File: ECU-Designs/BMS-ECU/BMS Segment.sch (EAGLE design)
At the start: 94 parts, among them Q10 P-CHANNEL_MOSFET, Q11 P-CHANNEL_MOSFET, Q12 P-CHANNEL_MOSFET, Q13 P-CHANNEL_MOSFET, Q2 P-CHANNEL_MOSFET, Q3 P-CHANNEL_MOSFET, Q4 P-CHANNEL_MOSFET, Q5 P-CHANNEL_MOSFET, Q6 P-CHANNEL_MOSFET, Q7 P-CHANNEL_MOSFET, Q8 P-CHANNEL_MOSFET, Q9 P-CHANNEL_MOSFET

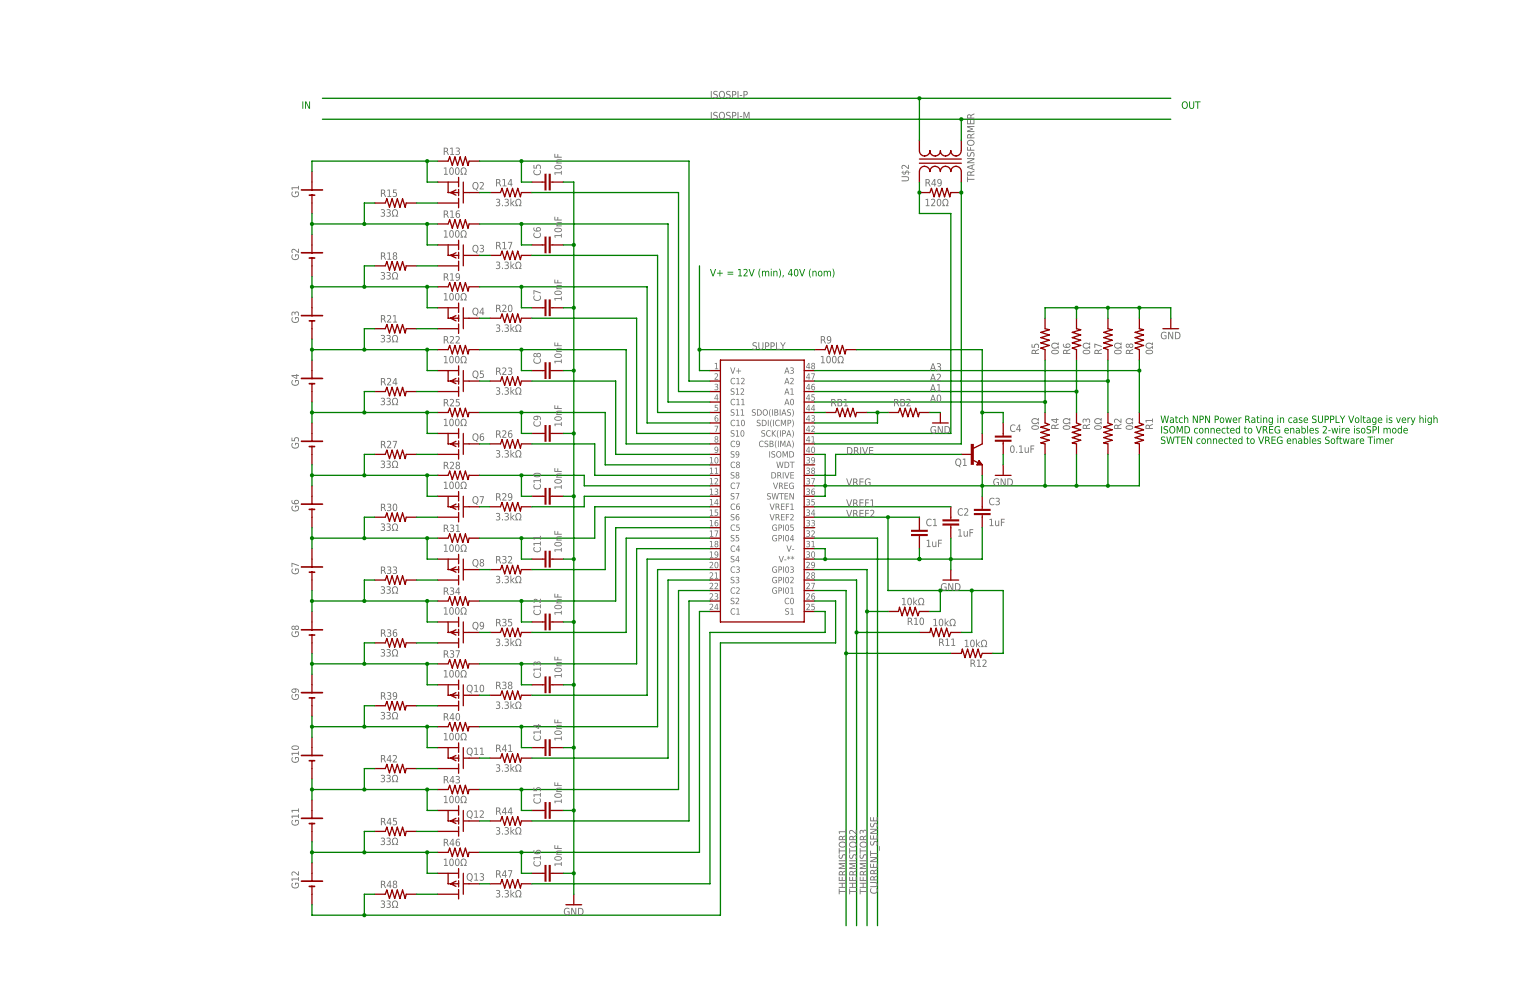
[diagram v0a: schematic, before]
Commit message: Updated BMS segment & created BMS Microcontroller
Updated BMS segment schematic to to reflect that the LTC6804 is powered
from the cells it is monitoring.  Also added connectors.  Created a
preliminary design for the microcontroller board that will process the
BMS data from all the BMS segment boards.  Some resistor values and pin
assignments still need to be determined.
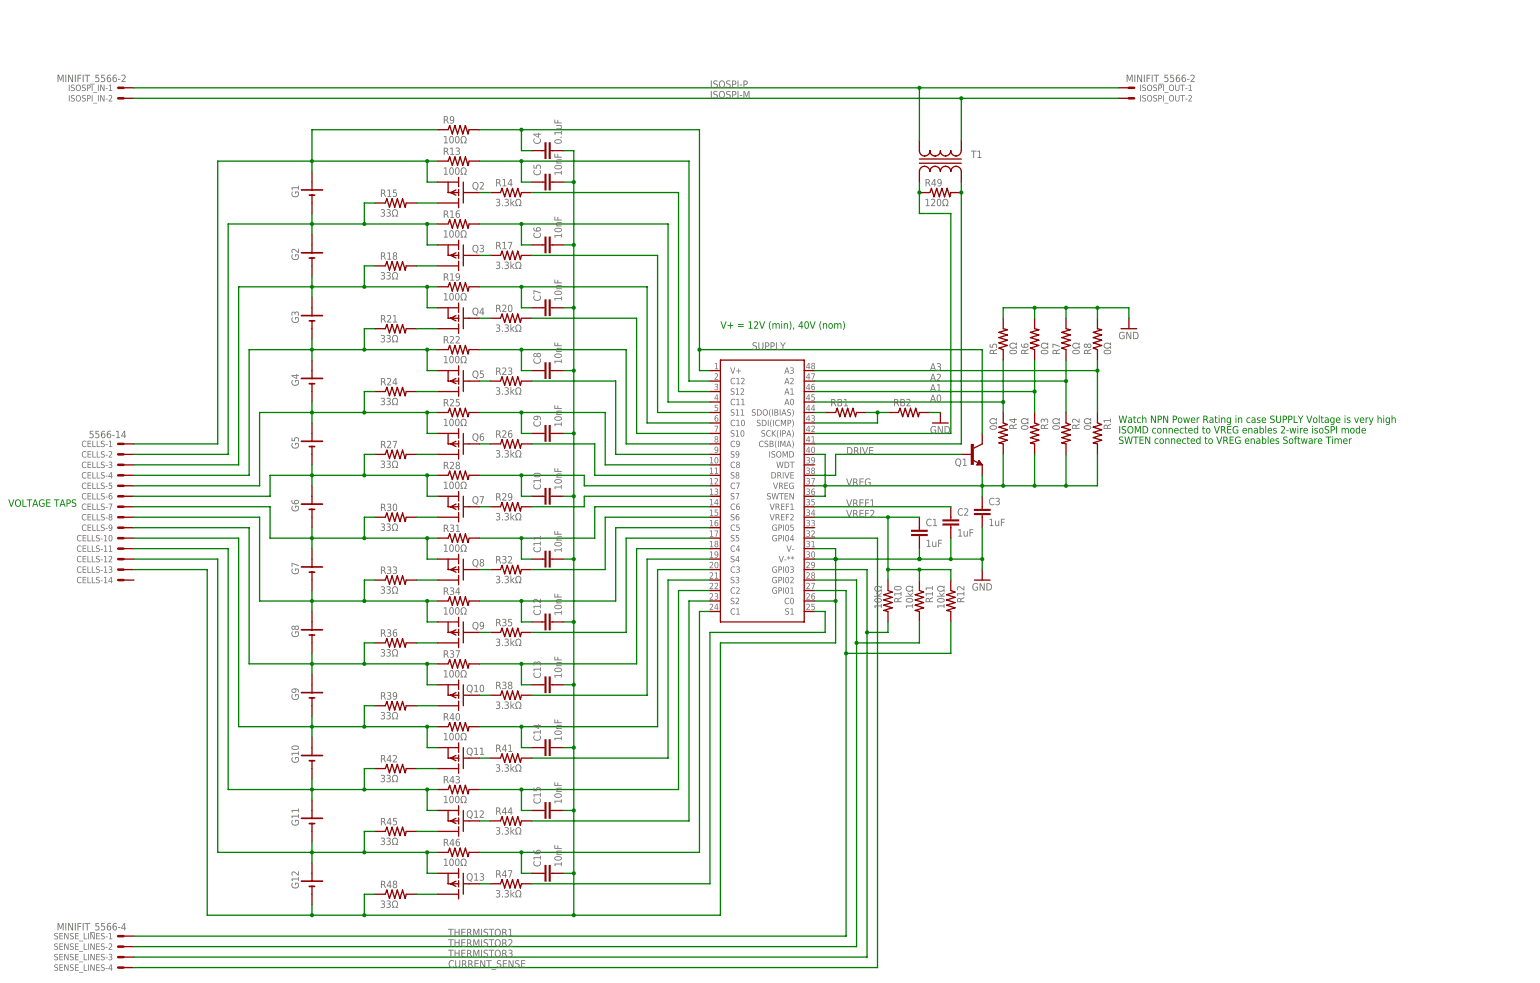
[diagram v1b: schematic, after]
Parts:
- added CELLS: 5566-14, con-molex:5566-14
- added ISOSPI_IN, ISOSPI_OUT: MINIFIT_5566-2, HyTechDevices:MINIFIT_5566-2
- added SENSE_LINES: MINIFIT_5566-4, HyTechDevices:MINIFIT_5566-4
- renumbered U$2 to T1
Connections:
- removed net N$5: C4.1, Q1.COLLECTOR, R9.2
- removed net N$67: G12.-, R48.1, U$1.C0
- net CURRENT_SENSE: now also SENSE_LINES-4.S
- net GND: now also CELLS-13.S, G12.-, R48.1, U$1.C0
- net ISOSPI-M: now also ISOSPI_IN-2.S, ISOSPI_OUT-2.S
- net ISOSPI-P: now also ISOSPI_IN-1.S, ISOSPI_OUT-1.S
- net N$19: now also CELLS-2.S
- net N$21: now also CELLS-3.S
- net N$26: now also CELLS-4.S
- net N$3: now also CELLS-1.S, R9.1
- net N$33: now also CELLS-5.S
- net N$37: now also CELLS-6.S
- net N$41: now also CELLS-7.S
- net N$44: now also CELLS-8.S
- net N$47: now also CELLS-9.S
- net N$54: now also CELLS-10.S
- net N$60: now also CELLS-11.S
- net N$63: now also CELLS-12.S
- net SUPPLY: now also C4.1, Q1.COLLECTOR, R9.2; no longer R9.1
- net THERMISTOR1: now also SENSE_LINES-1.S
- net THERMISTOR2: now also SENSE_LINES-2.S
- net THERMISTOR3: now also SENSE_LINES-3.S
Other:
- note added: "VOLTAGE TAPS"
- note removed: "IN"
- note removed: "OUT"
- moved on the sheet: C4, R1, R10, R11, R12, R2, R3, R4, R5, R6, R7, R8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

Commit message: Updated BMS Segment Schematic
Added newly created components from HyTechDevices Library and made a few
other small alterations to schematic (Reconfigured filtering capacitors,
fixed supply power for VREG, converted segments to daisy chain
configuration)
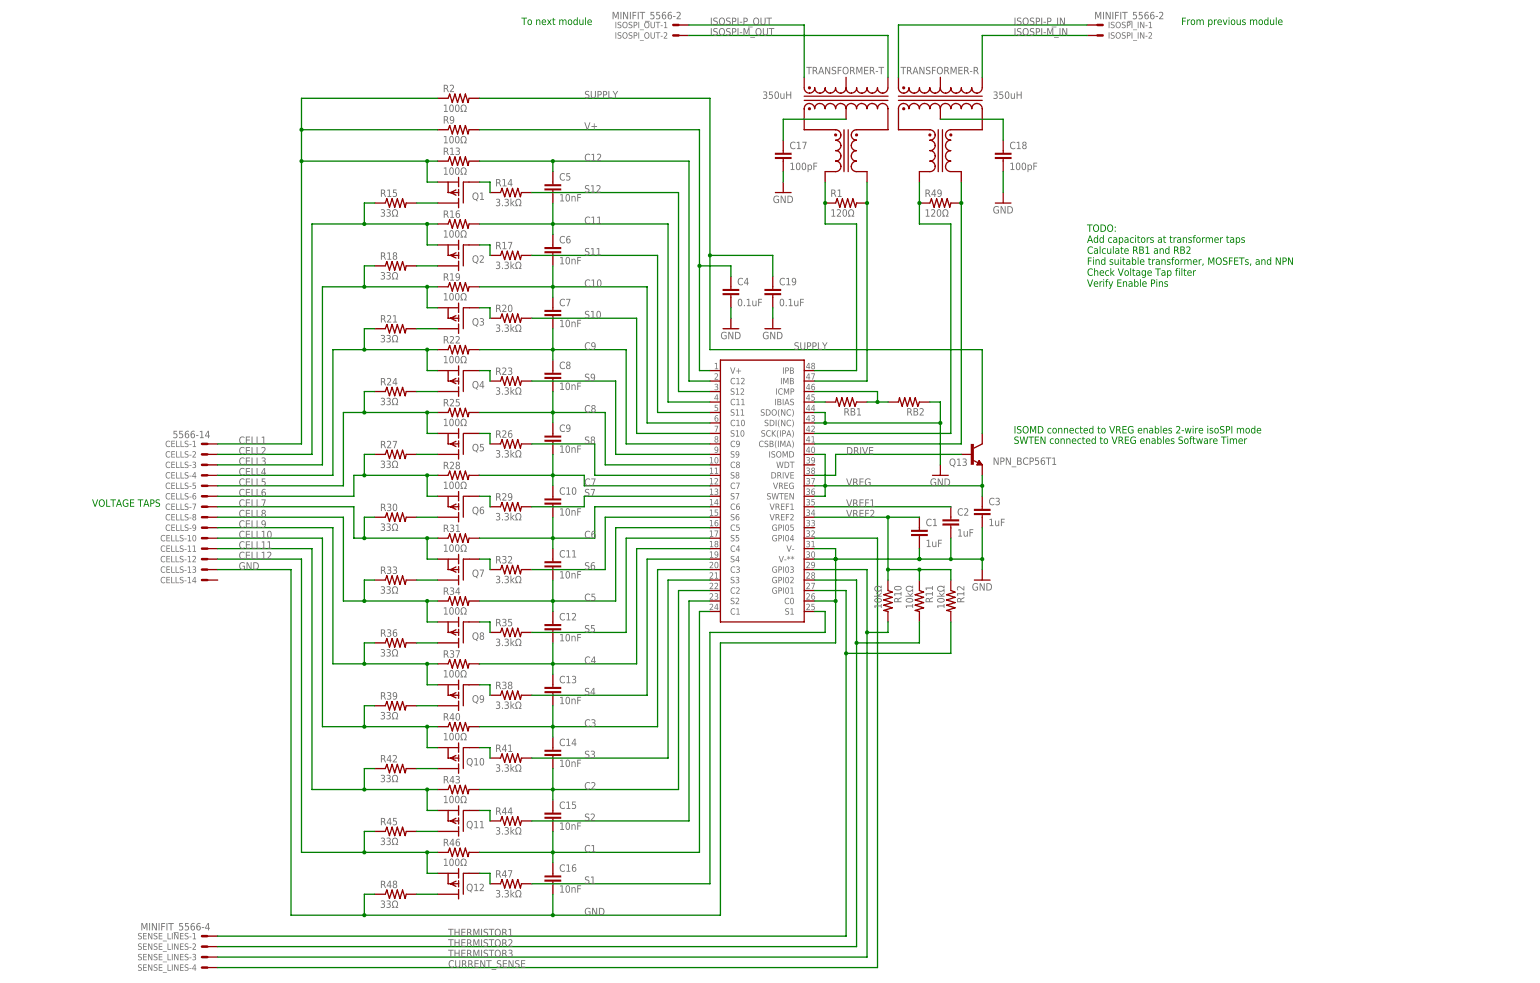
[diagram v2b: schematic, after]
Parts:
- removed G1, G10, G11, G12, G2, G3, G4, G5, G6, G7, G8, G9: BATTERY_1_CELL, HyTechSymbols:BATTERY_1_CELL
- removed R3, R4, R5, R6, R7, R8: 0Ω, HyTechDevices:RESISTOR0805-RES
- removed T1: TRANSFORMER, HyTechDevices:TRANSFORMER
- removed U$1: LTC6804-2, HyTechDevices:LTC6804-2
- added C17, C18: 100pF, HyTechDevices:CAP0805
- added C19: 0.1uF, HyTechDevices:CAP0805
- added TRANSFORMER-: 350uH, HyTechDevices:TRANSFORMER_749010013
- added U$2: (no value), HyTechDevices:LTC6804-1
- Q1: value (none) -> P-CHANNEL_MOSFET_DMP3099L-7; device HyTechDevices:BJT_NPNTIP120 -> HyTechDevices:P-CHANNEL_MOSFET_DMP3099L-7
- Q10, Q11, Q12, Q2, Q3, Q4, Q5, Q6, Q7, Q8, Q9: value P-CHANNEL_MOSFET -> P-CHANNEL_MOSFET_DMP3099L-7; device HyTechDevices:P-CHANNEL_MOSFET -> HyTechDevices:P-CHANNEL_MOSFET_DMP3099L-7
- Q13: value P-CHANNEL_MOSFET -> NPN_BCP56T1; device HyTechDevices:P-CHANNEL_MOSFET -> HyTechDevices:NPN_BCP56T1
- R1: value 0Ω -> 120Ω
- R15, R18, R21, R24, R27, R30, R33, R36, R39, R42, R45, R48: device HyTechDevices:RESISTOR0805-RES -> HyTechDevices:RESISTOR2512
- R2: value 0Ω -> 100Ω
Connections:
- removed net A0: R4.1, R5.1, U$1.A0
- removed net A1: R3.1, R6.1, U$1.A1
- removed net A2: R2.1, R7.1, U$1.A2
- removed net A3: R1.1, R8.1, U$1.A3
- removed net ISOSPI-M: ISOSPI_IN-2.S, ISOSPI_OUT-2.S, T1.S2
- removed net ISOSPI-P: ISOSPI_IN-1.S, ISOSPI_OUT-1.S, T1.S1
- removed net N$11: C6.1, R16.2, U$1.C11
- removed net N$14: R17.2, U$1.S11
- removed net N$16: C7.1, R19.2, U$1.C10
- removed net N$17: R20.2, U$1.S10
- removed net N$19: CELLS-2.S, G1.-, G2.+, Q3.S, R15.1, R16.1
- removed net N$21: CELLS-3.S, G2.-, G3.+, Q4.S, R18.1, R19.1
- removed net N$23: C8.1, R22.2, U$1.C9
- removed net N$24: R23.2, U$1.S9
- removed net N$26: CELLS-4.S, G3.-, G4.+, Q5.S, R21.1, R22.1
- removed net N$3: CELLS-1.S, G1.+, Q2.S, R13.1, R9.1
- removed net N$31: C9.1, R25.2, U$1.C8
- removed net N$32: R26.2, U$1.S8
- removed net N$33: CELLS-5.S, G4.-, G5.+, Q6.S, R24.1, R25.1
- removed net N$34: C10.1, R28.2, U$1.C7
- removed net N$35: R29.2, U$1.S7
- removed net N$37: CELLS-6.S, G5.-, G6.+, Q7.S, R27.1, R28.1
- removed net N$39: C11.1, R31.2, U$1.C6
- removed net N$40: R32.2, U$1.S6
- removed net N$41: CELLS-7.S, G6.-, G7.+, Q8.S, R30.1, R31.1
- removed net N$44: CELLS-8.S, G7.-, G8.+, Q9.S, R33.1, R34.1
- removed net N$45: C12.1, R34.2, U$1.C5
- removed net N$46: R35.2, U$1.S5
- removed net N$47: CELLS-9.S, G8.-, G9.+, Q10.S, R36.1, R37.1
- removed net N$49: C13.1, R37.2, U$1.C4
- removed net N$50: R38.2, U$1.S4
- removed net N$54: CELLS-10.S, G10.+, G9.-, Q11.S, R39.1, R40.1
- removed net N$55: C14.1, R40.2, U$1.C3
- removed net N$56: R41.2, U$1.S3
- removed net N$58: C15.1, R43.2, U$1.C2
- removed net N$59: R44.2, U$1.S2
- removed net N$60: CELLS-11.S, G10.-, G11.+, Q12.S, R42.1, R43.1
- removed net N$63: CELLS-12.S, G11.-, G12.+, Q13.S, R45.1, R46.1
- removed net N$64: C16.1, R46.2, U$1.C1
- removed net N$65: R47.2, U$1.S1
- new net C1: C15.2, C16.1, R46.2, U$2.C1
- new net C10: C6.2, C7.1, R19.2, U$2.C10
- new net C11: C5.2, C6.1, R16.2, U$2.C11
- new net C12: C5.1, R13.2, U$2.C12
- new net C2: C14.2, C15.1, R43.2, U$2.C2
- new net C3: C13.2, C14.1, R40.2, U$2.C3
- new net C4: C12.2, C13.1, R37.2, U$2.C4
- new net C5: C11.2, C12.1, R34.2, U$2.C5
- new net C6: C10.2, C11.1, R31.2, U$2.C6
- new net C7: C10.1, C9.2, R28.2, U$2.C7
- new net C8: C8.2, C9.1, R25.2, U$2.C8
- new net C9: C7.2, C8.1, R22.2, U$2.C9
- new net CELL1: CELLS-1.S, Q1.S, R13.1, R2.1, R9.1
- new net CELL10: CELLS-10.S, Q10.S, R39.1, R40.1
- new net CELL11: CELLS-11.S, Q11.S, R42.1, R43.1
- new net CELL12: CELLS-12.S, Q12.S, R45.1, R46.1
- new net CELL2: CELLS-2.S, Q2.S, R15.1, R16.1
- new net CELL3: CELLS-3.S, Q3.S, R18.1, R19.1
- new net CELL4: CELLS-4.S, Q4.S, R21.1, R22.1
- new net CELL5: CELLS-5.S, Q5.S, R24.1, R25.1
- new net CELL6: CELLS-6.S, Q6.S, R27.1, R28.1
- new net CELL7: CELLS-7.S, Q7.S, R30.1, R31.1
- new net CELL8: CELLS-8.S, Q8.S, R33.1, R34.1
- new net CELL9: CELLS-9.S, Q9.S, R36.1, R37.1
- new net ISOSPI-M_IN: ISOSPI_IN-2.S, TRANSFORMER-R.D-
- new net ISOSPI-M_OUT: ISOSPI_OUT-2.S, TRANSFORMER-T.D-
- new net ISOSPI-P_IN: ISOSPI_IN-1.S, TRANSFORMER-R.D+
- new net ISOSPI-P_OUT: ISOSPI_OUT-1.S, TRANSFORMER-T.D+
- new net N$42: R1.2, TRANSFORMER-T.X-, U$2.IMB
- new net N$5: R1.1, TRANSFORMER-T.X+, U$2.IPB
- new net S1: R47.2, U$2.S1
- new net S10: R20.2, U$2.S10
- new net S11: R17.2, U$2.S11
- new net S12: R14.2, U$2.S12
- new net S2: R44.2, U$2.S2
- new net S3: R41.2, U$2.S3
- new net S4: R38.2, U$2.S4
- new net S5: R35.2, U$2.S5
- new net S6: R32.2, U$2.S6
- new net S7: R29.2, U$2.S7
- new net S8: R26.2, U$2.S8
- new net S9: R23.2, U$2.S9
- new net V+: C4.1, R9.2, U$2.V+
- net CURRENT_SENSE: now also U$2.GPI04; no longer U$1.GPI04
- net DRIVE: now also Q13.BASE, U$2.DRIVE; no longer Q1.BASE, U$1.DRIVE
- net GND: now also C17.2, C18.2, C19.2, RB2.1, U$2.C0, U$2.SDI(NC), U$2.SDO(NC), U$2.V-, U$2.V-**; no longer C10.2, C11.2, C12.2, C13.2, C14.2, C15.2, C5.2, C6.2, C7.2, C8.2, C9.2, G12.-, R5.2, R6.2, R7.2, R8.2, RB2.2, U$1.C0, U$1.V-, U$1.V-**
- net N$1: now also C18.1, TRANSFORMER-R.CX; no longer C5.1, R13.2, U$1.C12
- net N$10: now also Q1.G; no longer Q2.G
- net N$12: now also Q2.G; no longer Q3.G
- net N$13: now also Q2.D; no longer Q3.D
- net N$15: now also Q3.G; no longer Q4.G
- net N$18: now also Q3.D; no longer Q4.D
- net N$2: now also C17.1, TRANSFORMER-T.CX; no longer R14.2, U$1.S12
- net N$20: now also Q8.G; no longer Q9.G
- net N$22: now also Q9.G; no longer Q10.G
- net N$25: now also Q4.D; no longer Q5.D
- net N$27: now also Q10.G; no longer Q11.G
- net N$28: now also Q11.G; no longer Q12.G
- net N$29: now also Q12.G; no longer Q13.G
- net N$30: now also Q5.D; no longer Q6.D
- net N$36: now also Q6.D; no longer Q7.D
- net N$38: now also Q7.D; no longer Q8.D
- net N$4: now also RB1.2, U$2.IBIAS; no longer RB1.1, U$1.SDO(IBIAS)
- net N$43: now also Q8.D; no longer Q9.D
- net N$51: now also Q9.D; no longer Q10.D
- net N$53: now also Q10.D; no longer Q11.D
- net N$6: now also Q1.D; no longer Q2.D
- net N$61: now also Q11.D; no longer Q12.D
- net N$66: now also Q12.D; no longer Q13.D
- net N$68: now also Q4.G; no longer Q5.G
- net N$69: now also Q5.G; no longer Q6.G
- net N$7: now also RB1.1, RB2.2, U$2.ICMP; no longer RB1.2, RB2.1, U$1.SDI(ICMP)
- net N$70: now also Q6.G; no longer Q7.G
- net N$71: now also Q7.G; no longer Q8.G
- net N$8: now also TRANSFORMER-R.X+, U$2.SCK(IPA); no longer T1.P1, U$1.SCK(IPA)
- net N$9: now also TRANSFORMER-R.X-, U$2.CSB(IMA); no longer T1.P2, U$1.CSB(IMA)
- net SUPPLY: now also C19.1, Q13.COLLECTOR, R2.2; no longer C4.1, Q1.COLLECTOR, R9.2, U$1.V+
- net THERMISTOR1: now also U$2.GPI01; no longer U$1.GPI01
- net THERMISTOR2: now also U$2.GPI02; no longer U$1.GPI02
- net THERMISTOR3: now also U$2.GPI03; no longer U$1.GPI03
- net VREF1: now also U$2.VREF1; no longer U$1.VREF1
- net VREF2: now also U$2.VREF2; no longer U$1.VREF2
- net VREG: now also Q13.EMITTER, U$2.ISOMD, U$2.SWTEN, U$2.VREG; no longer Q1.EMITTER, R1.2, R2.2, R3.2, R4.2, U$1.ISOMD, U$1.SWTEN, U$1.VREG
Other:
- note added: "From previous module"
- note added: "TODO: Add capacitors at transformer taps Calculate RB1 and RB2 Find suitable transformer, MOSFETs, and NPN Check Voltage Tap filter Verify Enable Pins"
- note added: "To next module"
- note removed: "V+ = 12V (min), 40V (nom)"
- note removed: "Watch NPN Power Rating in case SUPPLY Voltage is very high"
- moved on the sheet: C10, C11, C12, C13, C14, C15, C16, C4, C5, C6, C7, C8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

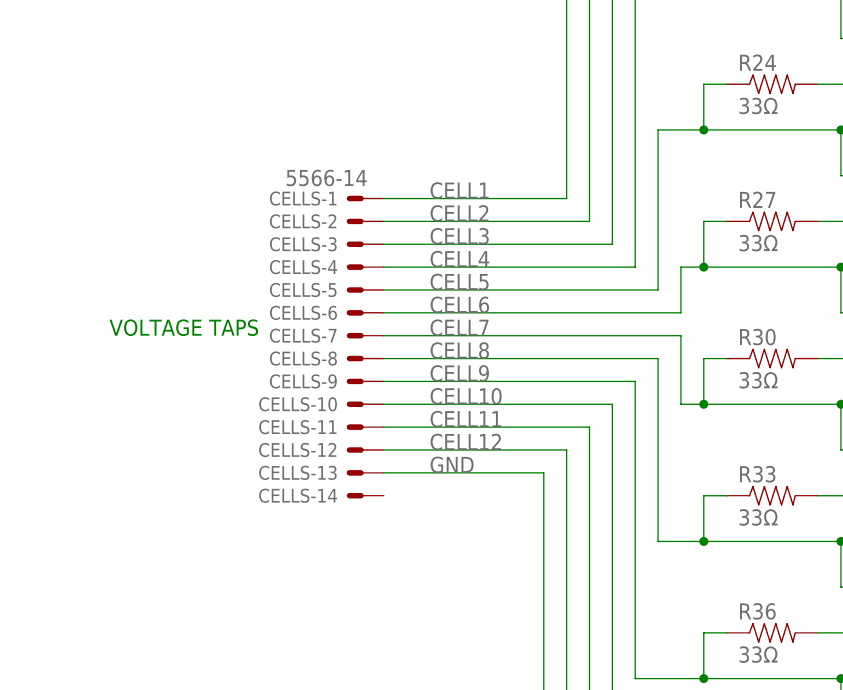
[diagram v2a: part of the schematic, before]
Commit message: Added fuses and spring contacts to BMS schematic
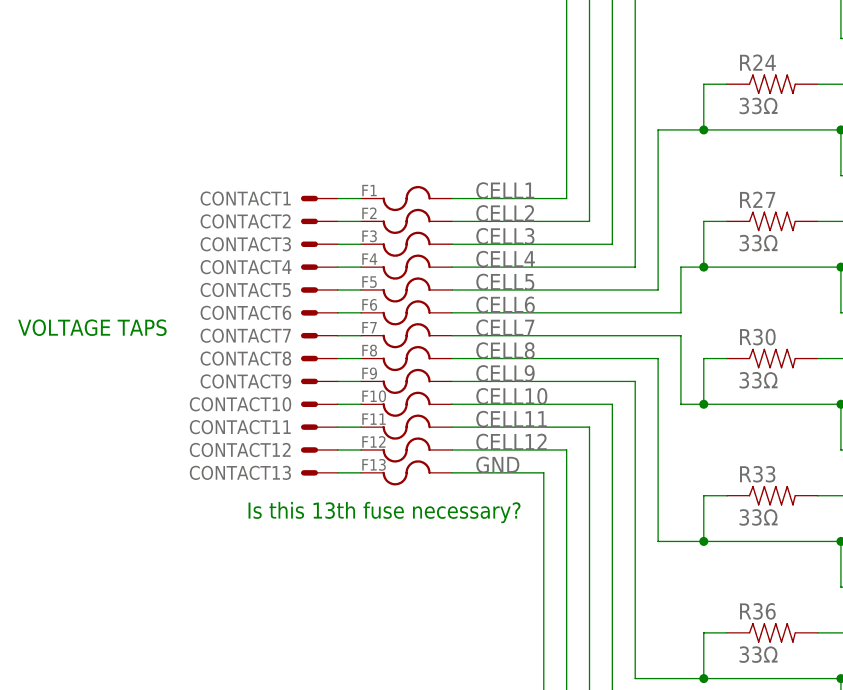
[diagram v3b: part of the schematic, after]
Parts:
- removed CELLS: 5566-14, con-molex:5566-14
- added CONTACT1, CONTACT10, CONTACT11, CONTACT12, CONTACT13, CONTACT2, CONTACT3, CONTACT4, CONTACT5, CONTACT6, CONTACT7, CONTACT8, CONTACT9: SPRING_CONTACT, HyTechDevices:SPRING_CONTACT
- added F1, F10, F11, F12, F13, F2, F3, F4, F5, F6, F7, F8, F9: C1Q_FUSE, HyTechDevices:C1Q_FUSE
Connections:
- new net N$11: CONTACT2.S, F2.1
- new net N$14: CONTACT3.S, F3.1
- new net N$16: CONTACT4.S, F4.1
- new net N$17: CONTACT5.S, F5.1
- new net N$19: CONTACT6.S, F6.1
- new net N$21: CONTACT7.S, F7.1
- new net N$23: CONTACT8.S, F8.1
- new net N$24: CONTACT9.S, F9.1
- new net N$26: CONTACT10.S, F10.1
- new net N$3: CONTACT1.S, F1.1
- new net N$31: CONTACT11.S, F11.1
- new net N$32: CONTACT12.S, F12.1
- new net N$33: CONTACT13.S, F13.1
- net CELL1: now also F1.2; no longer CELLS-1.S
- net CELL10: now also F10.2; no longer CELLS-10.S
- net CELL11: now also F11.2; no longer CELLS-11.S
- net CELL12: now also F12.2; no longer CELLS-12.S
- net CELL2: now also F2.2; no longer CELLS-2.S
- net CELL3: now also F3.2; no longer CELLS-3.S
- net CELL4: now also F4.2; no longer CELLS-4.S
- net CELL5: now also F5.2; no longer CELLS-5.S
- net CELL6: now also F6.2; no longer CELLS-6.S
- net CELL7: now also F7.2; no longer CELLS-7.S
- net CELL8: now also F8.2; no longer CELLS-8.S
- net CELL9: now also F9.2; no longer CELLS-9.S
- net GND: now also F13.2; no longer CELLS-13.S
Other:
- note added: "Is this 13th fuse necessary?"
